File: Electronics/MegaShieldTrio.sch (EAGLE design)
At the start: 29 parts, among them J2 RJ11-2L-B, X1 RJ45-6L21-B, X2 Cruise

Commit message: New sonar board; trio modified to match
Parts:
- removed ADCL2: Analog In 0-7, pinhead:PINHD-1X8
- added COMMUN: Digital 14-21, pinhead:PINHD-1X8
- added JP15: (no value), pinhead:PINHD-1X10
- ADCL: value Digital 14-21 -> Analog In 0-7
- renumbered ADCL1 to PWML
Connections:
- new net N$2: COMMUN.2, PWML.3
- new net N$9: COMMUN.1, PWML.4
- net +5V: now also X1.1; no longer X1.2
- net A6: now also COMMUN.7; no longer ADCL.7
- net D3INT1: now also COMMUN.8; no longer ADCL.8
- net GND: now also X1.4; no longer X1.1
- net N$11: now also COMMUN.4; no longer ADCL.4
- net N$25: now also ADCL.5, X1.7; no longer ADCL2.5, X1.5
- net N$26: now also ADCL.6, X1.3; no longer ADCL2.6, X1.6
- net N$33: now also COMMUN.3; no longer ADCL.3
- net N$34: now also ADCL.7, X1.5; no longer ADCL2.7, X1.7
- net N$35: now also ADCL.8; no longer ADCL2.8
- net N$36: now also X1.2; no longer X1.3
- net N$7: now also ADCL.4, X1.6; no longer ADCL2.4, X1.4
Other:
- note added: "3.3v"
- note added: "3V"
- note added: "D1 (Tx2)"
- note added: "D2 (Rx2)"
- note added: "D3 (MOSI)"
- note added: "D4 (MISO)"
- note added: "D5 (SCK)"
- note added: "D6 (SS)"
- note added: "GND"
- note added: "MISO"
- note added: "MOSI"
- note added: "NCS"
- note added: "NPO"
- note added: "Pgm"
- note added: "RST"
- note added: "Rx"
- note added: "SCLK"
- note added: "Tx"
- moved on the sheet: ADCL, JP11, JP12, JP13

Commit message: Parts match physical size
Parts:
- removed ADCH: Analog In 8-15, pinhead:PINHD-1X8
- removed ADCL: Analog In 0-7, pinhead:PINHD-1X8
- removed ADCL4, PWMH: Digital 8-13, pinhead:PINHD-1X8
- removed COMMUN: Digital 14-21, pinhead:PINHD-1X8
- removed J1: (no value), con-jack:JACK-PLUG0
- removed J2: RJ11-2L-B, con-tycoelectronics:RJ11-2L-B
- removed JP1, JP2: 5V, pinhead:PINHD-1X1
- removed JP10: (no value), pinhead:PINHD-1X4
- removed JP11: (no value), pinhead:PINHD-1X9
- removed JP12, JP13: (no value), pinhead:PINHD-1X2
- removed JP14: (no value), pinhead:PINHD-2X4
- removed JP15: (no value), pinhead:PINHD-1X10
- removed JP3, JP4: GND, pinhead:PINHD-1X1
- removed JP6: C3 Analog, pinhead:PINHD-1X15
- removed JP8: C4 Analog, pinhead:PINHD-1X15
- removed JP9: (no value), pinhead:PINHD-1X6
- removed PWML: Digital 0-7, pinhead:PINHD-1X8
- removed XIOH: Digital 22-37, pinhead:PINHD-2X8
- removed XIOL: Digital 38-53, pinhead:PINHD-2X8
- added C3A: C3 Analog, pinhead:PINHD-1X15
- added C3A2, C3D2, C4A2, C4D2: 1X15HEADER, Elcano:1X15HEADER
- added C4A: C4 Analog, pinhead:PINHD-1X15
- added C4SA0-5: Nano shield, Elcano:1X6HEADER
- added C4SD8-13: Nano shield, Elcano:PINHD-1X8SMALL8
- added C4SPWR: Nano shield, pinhead:PINHD-1X5
- added C5A: C5 Analog, pinhead:PINHD-1X15
- added C6A0-7: C6 Analog In 0-7, pinhead:PINHD-1X8
- added C6A8-15: C6 Analog In 8-15, pinhead:PINHD-1X8
- added C6D0-7: GPS, pinhead:PINHD-1X8
- added C6D14-21: C6 Digital 14-21, pinhead:PINHD-1X8
- added C6D14-21_2: C5D, Elcano:PINHD-1X8SMALL8
- added C6D22-37: C6 Digital 22-37, pinhead:PINHD-2X9
- added C6D38-53: C6 Digital 38-53, pinhead:PINHD-2X9
- added C6D70-77, C6D78-85: Max32, pinhead:PINHD-2X8
- added C6D8-13: C6D8-13, pinhead:PINHD-1X8
- added ICSP: (no value), pinhead:PINHD-2X3
- added MOUSE: Visual odometry, pinhead:PINHD-1X10
- added R2, R3: 1 M, rcl:R-US_0207/10
- added RL1: V23040--B201TSC, Elcano:V23040--B201TSC
- added U$4: CHR_UM6, Elcano:CHR_UM6
- added X3: ODO_JACK, Elcano:ODO_JACK
- added X4, X5: RJ45-8L-B, con-tycoelectronics:RJ45-8L-B
- C4SD0-7: value Digital 0-7 -> Nano shield
- POWER: value POWER -> C6 Power; device pinhead:PINHD-1X6 -> pinhead:PINHD-1X8
- R1: value 1M -> 1 M; device rcl:R-US_0204/5 -> rcl:R-US_0207/10
- X1: value RJ45-6L21-B -> Vehicle control; device con-tycoelectronics:RJ45-6L21-B -> con-subd:M25H
- X2: value Cruise -> ODO_JACK; device con-subd:F25H -> Elcano:ODO_JACK
- renumbered ADCL3 to C4SD0-7, JP5 to C3D, JP7 to C4D
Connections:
- removed net A12: JP6.5, PWMH.1, X2.10
- removed net A13: ADCH.6, C3D.14, X2.6
- removed net A14: ADCH.7, C3D.13, X2.7
- removed net A15: ADCH.8, C3D.12, X2.8
- removed net A6: COMMUN.7, X2.23
- removed net D23: X2.5, XIOH.15
- removed net D27: JP6.15, X2.4, XIOH.11
- removed net D29: ADCL4.6, JP8.15, X2.3, XIOH.9
- removed net D31: X2.2, XIOH.7
- removed net D33: X2.1, XIOH.5
- removed net D35: JP14.7, X2.15, XIOH.3
- removed net D36: X2.13, XIOH.2
- removed net D37: X2.16, XIOH.1
- removed net D3INT1: COMMUN.8, J1.3, R1.2, X2.21
- removed net D43: XIOL.11
- removed net D49: J2.1, XIOL.5
- removed net D53: J2.3, XIOL.1
- removed net D9: JP6.6, PWMH.2
- removed net N$1: PWML.1, X2.19
- removed net N$2: COMMUN.2, PWML.3
- removed net N$27: ADCL4.8, JP8.13
- removed net N$6: J2.4, XIOL.2
- new net AREF: C3A.13, C3A2.13, C4A.13, C4A2.13, C4SD8-13.1, C5A.13, C6D8-13.1
- new net CRS_BRAKE: C3D.13, C3D2.13, C5A.6, C6A8-15.7, X1.7
- new net CRS_DRIVE_CMD: C3D.2, C3D2.2, X1.18
- new net CRS_REVERSE: C3D.11, C3D2.11, C6D22-37.2, X1.13
- new net CRS_STEER: C3D.14, C3D2.14, C5A.7, C6A8-15.6, X1.6
- new net CRS_THROTTLE: C3D.12, C3D2.12, C5A.5, C6A8-15.8, X1.8
- new net DIRECTION: C3A.6, C3A2.6
- new net HORIZ: C4A.5, C4A2.5, C4SA0-5.1
- new net LED1: C6D22-37.15, X1.5
- new net LED3: C3A.15, C3A2.15, C6D22-37.11, X1.4
- new net LED4: C4A.15, C4A2.15, C4SD8-13.3, C6D22-37.9, X1.3
- new net LED5: C6D22-37.7, X1.2
- new net LED6: C6D22-37.5, X1.1
- new net LED7: C6D22-37.3, X1.15
- new net LED8: C6D22-37.1, X1.16
- new net MISO: C6D38-53.13, ICSP.1, MOUSE.5, U$4.7
- new net MOSI: C6D38-53.14, ICSP.4, MOUSE.6, U$4.8
- new net MOUSE_LED: C6D38-53.12, MOUSE.10
- new net MOUSE_SS: C6D38-53.16, MOUSE.4
- new net N$29: C3D.9, C3D2.9, RL1K.2
- new net N$30: C6D78-85.7, C6D78-85.8
- new net N$31: C6D78-85.10, C6D78-85.9
- new net N$32: RL1K1.5, X4.1, X5.1
- new net N$39: C6D78-85.15, C6D78-85.16
- new net N$41: C6D70-77.1, C6D70-77.2
- new net N$42: C6D0-7.6, C6D14-21.2, C6D14-21_2.7, U$4.9
- new net N$43: C6D14-21.6, C6D14-21_2.3, U$4.13
- new net N$44: C6D70-77.3, C6D70-77.4
- new net N$45: C6D70-77.5, C6D70-77.6
- new net N$46: C6D70-77.7, C6D70-77.8
- new net N$47: C6D70-77.10, C6D70-77.9
- new net N$48: C6D70-77.11, C6D70-77.12
- new net N$49: C6D70-77.13, C6D70-77.14
- new net N$50: C6D70-77.15, C6D70-77.16
- new net N$52: C4A.14, C4A2.14
- new net N$54: C3D.6, C3D2.6
- new net N$55: C3D.10, C3D2.10
- new net N$56: C3A.1, C3A2.1, C5A.1, C6D22-37.13, POWER.1
- new net N$57: C3A.7, C3A2.7
- new net N$59: C3A.14, C3A2.14
- new net NPD: C6D38-53.10, MOUSE.9
- new net PRESENCE: C4A.8, C4A2.8, C4SA0-5.4
- new net RX0: C6D0-7.8, X1.22
- new net SCK: C6D38-53.15, ICSP.3, MOUSE.7, U$4.6
- new net SIZE: C4A.7, C4A2.7, C4SA0-5.3
- new net SPEED: C3A.5, C3A2.5, C6D8-13.7, X1.10
- new net SPEED_LIMIT: C4D.7, C4D2.7, C4SD0-7.5, X1.9
- new net TILT_SS: C6D38-53.8, U$4.5
- new net TX0: C6D0-7.7, X1.20
- new net VBIT0: C4D.8, C4D2.8, C4SD0-7.6, C6D38-53.3
- new net VBIT1: C4D.9, C4D2.9, C4SD0-7.7, C6D38-53.5
- new net VBIT2: C4D.10, C4D2.10, C4SD0-7.8, C6D38-53.7
- new net VBIT3: C4D.11, C4D2.11, C4SD8-13.8, C6D38-53.9
- new net VERT: C4A.6, C4A2.6, C4SA0-5.2
- new net VIS_VALID: C4D.15, C4D2.15, C4SD8-13.4, C6D38-53.11
- new net WHEEL_CLICK: C6D14-21.8, C6D14-21_2.1, R2.1, X1.21, X3.1
- new net WIRELESS: C6D14-21.7, C6D14-21_2.2, R1.1, X1.14, X2.1
- net +5V: now also C3A.4, C3A2.4, C4A.4, C4A2.4, C4SPWR.3, C5A.4, C6D22-37.17, C6D22-37.18, ICSP.2, MOUSE.2, POWER.4, R1.2, R2.2, R3.2, RL1K1.6, U$4.1, X1.24; no longer JP1.1, JP10.3, JP2.1, JP6.4, JP8.4, POWER.3, R1.1, X1.1, X2.24
- net D39: now also C6D38-53.2, X1.12; no longer X2.12, XIOL.15
- net D41: now also C6D38-53.4, X1.11; no longer X2.11, XIOL.13
- net GND: now also C3A.2, C3A2.2, C3D2.4, C4A.2, C4A2.2, C4D2.4, C4SD8-13.2, C4SPWR.4, C4SPWR.5, C5A.2, C6D38-53.17, C6D38-53.18, C6D8-13.2, ICSP.6, MOUSE.1, POWER.2, POWER.3, U$4.2, U$4.3, X1.25, X2.2, X2.3, X3.2, X3.3, X4.4, X5.4; no longer ADCL4.7, J1.1, J1.2, J2.6, JP10.4, JP3.1, JP4.1, JP6.2, JP8.2, POWER.4, POWER.5, PWMH.7, X1.4, X2.25
- net N$10: now also C3D2.1, C4D2.2
- net N$11: now also C4D2.5, C6D14-21.4, C6D14-21_2.5; no longer COMMUN.4
- net N$12: now also C3D2.5, C4D2.6
- net N$13: now also C3D.7, C3D2.7, X5.2; no longer C4D.7, C4SD0-7.5
- net N$14: now also C5A.11, C6A8-15.2, X5.7; no longer J2.2, XIOL.3
- net N$15: now also C5A.10, C6A8-15.3, X5.6; no longer C3D.2, X2.18
- net N$16: now also C5A.9, C6A8-15.4, X5.5; no longer JP14.2, JP8.5, JP9.1
- net N$17: now also C6D14-21.5, C6D14-21_2.4, U$4.12; no longer C4D.10, C4SD0-7.8
- net N$18: now also C5A.8, C6A8-15.5, X5.3; no longer ADCL4.1, C4D.11
- net N$19: now also C4D2.12, C4SD8-13.7, C6A0-7.3; no longer ADCL4.2, JP14.1
- net N$20: now also C4D2.14, C4SD8-13.5, C6A0-7.1; no longer ADCL4.4, JP14.5
- net N$21: now also C5A.12, C6A8-15.1, X5.8; no longer JP14.4, JP8.6, JP9.2
- net N$22: now also C4A.1, C4A2.1; no longer JP14.6, JP8.7, JP9.3
- net N$23: now also C6D78-85.1, C6D78-85.2; no longer ADCL4.5, C4D.15
- net N$24: now also C6D78-85.3, C6D78-85.4; no longer JP14.8, JP8.8, JP9.4
- net N$25: now also C3A.9, C3A2.9, C4A.9, C4A2.9, C4SA0-5.5, C6A0-7.5, X4.7; no longer ADCL.5, JP6.9, JP8.9, JP9.5, X1.7
- net N$26: now also C3A.10, C3A2.10, C4A.10, C4A2.10, C4SA0-5.6, C6A0-7.6, X4.3; no longer ADCL.6, JP6.10, JP8.10, JP9.6, X1.3
- net N$28: now also C6D78-85.5, C6D78-85.6; no longer JP10.2, JP8.14
- net N$3: now also C4D2.13, C4SD8-13.6, C6A0-7.2; no longer ADCL4.3, JP14.3
- net N$33: now also C4D2.1, C6D14-21.3, C6D14-21_2.6; no longer COMMUN.3
- net N$34: now also C3A.11, C3A2.11, C4A.11, C4A2.11, C6A0-7.7, X4.5; no longer ADCL.7, JP6.11, JP8.11, X1.5
- net N$35: now also C3A.12, C3A2.12, C4A.12, C4A2.12, C6A0-7.8, X4.8; no longer ADCL.8, JP6.12, JP8.12, X1.8
- net N$36: now also C3D2.8, X4.2; no longer X1.2
- net N$37: now also C6D78-85.11, C6D78-85.12; no longer PWML.2, X2.20
- net N$38: now also C6D78-85.13, C6D78-85.14; no longer C4D.9, C4SD0-7.7
- net N$4: now also C3D2.15, C6D22-37.16, X1.17; no longer X2.17, XIOH.16
- net N$5: now also C4SPWR.2, MOUSE.3, POWER.5, RL1K1.4; no longer ADCH.1, C4D.8, C4SD0-7.6, X2.9
- net N$7: now also C3A.8, C3A2.8, C6A0-7.4, X4.6; no longer ADCL.4, JP6.8, X1.6
- net N$8: now also R3.1, RL1K.1; no longer J2.5, XIOL.4
- net N$9: now also C6D0-7.5, C6D14-21.1, C6D14-21_2.8, U$4.10; no longer COMMUN.1, PWML.4
- net RESET: now also C3A.3, C3A2.3, C3D2.3, C4A.3, C4A2.3, C4D2.3, C4SPWR.1, C5A.3, ICSP.5, MOUSE.8, POWER.6; no longer JP10.1, JP6.3, JP8.3, POWER.1
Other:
- note added: "3.3 V"
- note added: "5 V"
- note added: "5V / 3.3V power"
- note added: "Aref"
- note added: "CH Robotics UM6"
- note added: "Chain_2"
- note added: "D19 Rx1"
- note added: "F2"
- note added: "FL2"
- note added: "FR2"
- note added: "GPS Location"
- note added: "L2"
- note added: "NPD"
- note added: "Power 3/5"
- note added: "Presence"
- note added: "R2"
- note added: "SCK"
- note added: "Tilt SS"
- note added: "Vcc"
- note added: "Vision bit 0"
- note added: "Vision bit 1"
- note added: "Vision bit 2"
- note added: "Vision bit 3"
- note added: "Vision valid"
- note added: "Wireless"
- note removed: "(MOSI)"
- note removed: "3.3v"
- note removed: "Coneness"
- note removed: "D19 Tx1"
- note removed: "Female"
- note removed: "Power F"
- note removed: "SS"
- note removed: "Vision"
- moved on the sheet: R1

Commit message: Rearranged signals
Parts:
- added JP1, JP2, JP3: (no value), jumper:JP2E
- added JP4: (no value), Elcano:PINHD-1X8SMALL8
- ICSP: value (none) -> C6
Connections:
- net N$17 renamed INU_CNTRL
- net N$32 renamed SNR_PWR
- net N$43 renamed INU_BRN
- removed net CRS_BRAKE: C3D.13, C3D2.13, C5A.6, C6A8-15.7, X1.7
- removed net CRS_DRIVE_CMD: C3D.2, C3D2.2, X1.18
- removed net CRS_REVERSE: C3D.11, C3D2.11, C6D22-37.2, X1.13
- removed net CRS_STEER: C3D.14, C3D2.14, C5A.7, C6A8-15.6, X1.6
- removed net CRS_THROTTLE: C3D.12, C3D2.12, C5A.5, C6A8-15.8, X1.8
- removed net DIRECTION: C3A.6, C3A2.6
- removed net HORIZ: C4A.5, C4A2.5, C4SA0-5.1
- removed net MOUSE_LED: C6D38-53.12, MOUSE.10
- removed net N$10: C3D.1, C3D2.1, C4D.2, C4D2.2, C4SD0-7.2
- removed net N$11: C4D.5, C4D2.5, C4SD0-7.3, C6D14-21.4, C6D14-21_2.5
- removed net N$12: C3D.5, C3D2.5, C4D.6, C4D2.6, C4SD0-7.4
- removed net N$13: C3D.7, C3D2.7, X5.2
- removed net N$14: C5A.11, C6A8-15.2, X5.7
- removed net N$15: C5A.10, C6A8-15.3, X5.6
- removed net N$16: C5A.9, C6A8-15.4, X5.5
- removed net N$18: C5A.8, C6A8-15.5, X5.3
- removed net N$19: C4D.12, C4D2.12, C4SD8-13.7, C6A0-7.3
- removed net N$20: C4D.14, C4D2.14, C4SD8-13.5, C6A0-7.1
- removed net N$21: C5A.12, C6A8-15.1, X5.8
- removed net N$22: C4A.1, C4A2.1
- removed net N$25: C3A.9, C3A2.9, C4A.9, C4A2.9, C4SA0-5.5, C6A0-7.5, X4.7
- removed net N$26: C3A.10, C3A2.10, C4A.10, C4A2.10, C4SA0-5.6, C6A0-7.6, X4.3
- removed net N$29: C3D.9, C3D2.9, RL1K.2
- removed net N$3: C4D.13, C4D2.13, C4SD8-13.6, C6A0-7.2
- removed net N$33: C4D.1, C4D2.1, C4SD0-7.1, C6D14-21.3, C6D14-21_2.6
- removed net N$34: C3A.11, C3A2.11, C4A.11, C4A2.11, C6A0-7.7, X4.5
- removed net N$35: C3A.12, C3A2.12, C4A.12, C4A2.12, C6A0-7.8, X4.8
- removed net N$36: C3D.8, C3D2.8, X4.2
- removed net N$42: C6D0-7.6, C6D14-21.2, C6D14-21_2.7, U$4.9
- removed net N$52: C4A.14, C4A2.14
- removed net N$54: C3D.6, C3D2.6
- removed net N$55: C3D.10, C3D2.10
- removed net N$56: C3A.1, C3A2.1, C5A.1, C6D22-37.13, POWER.1
- removed net N$57: C3A.7, C3A2.7
- removed net N$59: C3A.14, C3A2.14
- removed net N$9: C6D0-7.5, C6D14-21.1, C6D14-21_2.8, U$4.10
- removed net PRESENCE: C4A.8, C4A2.8, C4SA0-5.4
- removed net RX0: C6D0-7.8, X1.22
- removed net SIZE: C4A.7, C4A2.7, C4SA0-5.3
- removed net SPEED_LIMIT: C4D.7, C4D2.7, C4SD0-7.5, X1.9
- removed net TILT_SS: C6D38-53.8, U$4.5
- removed net TX0: C6D0-7.7, X1.20
- removed net VBIT2: C4D.10, C4D2.10, C4SD0-7.8, C6D38-53.7
- removed net VBIT3: C4D.11, C4D2.11, C4SD8-13.8, C6D38-53.9
- removed net VERT: C4A.6, C4A2.6, C4SA0-5.2
- removed net VIS_VALID: C4D.15, C4D2.15, C4SD8-13.4, C6D38-53.11
- removed net WHEEL_CLICK: C6D14-21.8, C6D14-21_2.1, R2.1, X1.21, X3.1
- removed net WIRELESS: C6D14-21.7, C6D14-21_2.2, R1.1, X1.14, X2.1
- new net 3.3V: C3A.14, C3A2.14, C4A.14, C4A2.14, C4SPWR.2, MOUSE.3, POWER.5, RL1K1.4
- new net 4D5_6A14: C4D.8, C4D2.8, C4SD0-7.6
- new net 4D6_6A15: C4D.9, C4D2.9, C4SD0-7.7
- new net 4D7_6D43: C4D.10, C4D2.10, C4SD0-7.8, C6D38-53.6
- new net 6D10_2A6: C6D8-13.6, X1.23
- new net C2STAT: C6D14-21.4, C6D14-21_2.5, X1.19
- new net C4AVL: C3D.5, C3D2.5, C4D.6, C4D2.6, C4SD0-7.4, C6D22-37.3
- new net C4D11: C4D.14, C4D2.14, C4SD8-13.5
- new net C4D12: C4D.15, C4D2.15, C4SD8-13.4
- new net C6AVL: C4D.5, C4D2.5, C4SD0-7.3, C6D22-37.16
- new net C6D29: C6D22-37.10, JP4.1
- new net C6D31: C6D22-37.8, JP4.2
- new net C6D33: C6D22-37.6, JP4.3
- new net C6D35: C6D22-37.4, JP4.4
- new net C6D37: C6D22-37.2, JP4.5
- new net CHN1: C3D.7, C3D2.7, C6D38-53.1, X4.2
- new net CHN2: C3D.6, C3D2.6, C6D22-37.1, X5.2
- new net CLICK1: C6D0-7.6, R2.1, X1.21, X3.1
- new net CLICK2: C6D0-7.5, R1.1, X1.14, X2.1
- new net CRS_BRK: C3D.8, C3D2.8, C6A0-7.6, C6D0-7.3, C6D38-53.3, X1.7
- new net CRS_REV: C3D.11, C3D2.11, C6D38-53.9, X1.13
- new net CRS_STR: C3D.9, C3D2.9, C6A0-7.7, C6D38-53.5, X1.6
- new net CRS_THR: C3D.12, C3D2.12, C6A0-7.8, C6D38-53.11, C6D38-53.8, X1.8
- new net DRV_CMD: C3D.1, C3D2.1, C6D22-37.11, X1.18
- new net F2RNG: C3A.10, C3A2.10, C4A.10, C4A2.10, C4SA0-5.6, C5A.5, C6A8-15.8, X5.4
- new net FL2RNG: C5A.6, C6A8-15.7, X5.5
- new net FL_RNG: C3A.6, C3A2.6, C4A.6, C4A2.6, C4SA0-5.2, C6A0-7.2, X4.5
- new net FR2RNG: C5A.7, C6A8-15.6, X5.6
- new net FR_RNG: C3A.7, C3A2.7, C4A.7, C4A2.7, C4SA0-5.3, C6A0-7.3, X4.6
- new net F_RNG: C3A.5, C3A2.5, C4A.5, C4A2.5, C4SA0-5.1, C5A.10, C6A0-7.1, X4.4
- new net GPS_CNTRL: C6D14-21.1, C6D14-21_2.8, U$4.10
- new net GPS_LOC: C6D14-21.2, C6D14-21_2.7, U$4.9
- new net GPS_PWR: C6D8-13.7
- new net INU_SS: C6D22-37.12, U$4.5
- new net L2RNG: C3A.11, C3A2.11, C4A.11, C4A2.11, C5A.8, X5.7
- new net L_RNG: C3A.8, C3A2.8, C4A.8, C4A2.8, C4SA0-5.4, C5A.11, C6A0-7.4, X4.7
- new net MOV_OK: C3D.13, C3D2.13, C4SD0-7.5, C6D0-7.4, JP3.3, X1.17
- new net N$1: C4A.3, C4A2.3, C4D.3, C4D2.3, C4SPWR.1
- new net N$2: C4D.7, C4D2.7
- new net N$6: C6D38-53.17, JP2.2
- new net NAV_FIX: C4D.2, C4D2.2, C4SD0-7.1, C6D14-21.3, C6D14-21_2.6
- new net PATH: C3D.2, C3D2.2, C4D.1, C4D2.1, C4SD0-7.2, C6D22-37.9
- new net PWR_SEL: C3D.10, C3D2.10, C6D38-53.7, RL1K.2
- new net R2RNG: C3A.12, C3A2.12, C4A.12, C4A2.12, C5A.9, C6A8-15.4, X5.8
- new net R_RNG: C3A.9, C3A2.9, C4A.9, C4A2.9, C4SA0-5.5, C5A.12, C6A0-7.5, X4.8
- new net SPD_LMT: C4D.12, C4D2.12, C4SD8-13.7, X1.9
- new net VIN: C3A.1, C3A2.1, C4A.1, C4A2.1, C5A.1, C6D22-37.14, POWER.1
- new net VIS_IN: X1.20
- new net VIS_OUT: C6D0-7.7, X1.22
- net +5V: no longer C5A.4, R3.2
- net D39: now also C3D.15, C3D2.15, C4D.13, C4D2.13, C4SD8-13.6, JP4.6
- net D41: now also C4D.11, C4D2.11, C4SD8-13.8, JP2.3, JP4.7
- net GND: now also C6D22-37.5, JP2.1, X4.3, X5.3; no longer C6D38-53.17, X4.4, X5.4
- net LED1: now also C6D8-13.8; no longer C6D22-37.15
- net LED3: no longer C6D22-37.11
- net LED4: no longer C6D22-37.9
- net LED5: now also C5A.15, C6D38-53.12, MOUSE.10; no longer C6D22-37.7
- net LED6: now also C6D22-37.13; no longer C6D22-37.5
- net LED7: now also C6D22-37.15; no longer C6D22-37.3
- net LED8: now also C6D14-21.8, C6D14-21_2.1; no longer C6D22-37.1
- net MISO: now also C6D8-13.4, JP3.1; no longer C6D38-53.13
- net MOSI: now also C6D8-13.5
- net N$4: now also C6D38-53.15, JP1.2; no longer C3D.15, C3D2.15, C6D22-37.16, X1.17
- net N$5: now also C6D38-53.13, JP3.2; no longer C4SPWR.2, MOUSE.3, POWER.5, RL1K1.4
- net N$7: now also C6D14-21.7, C6D14-21_2.2; no longer C3A.8, C3A2.8, C6A0-7.4, X4.6
- net RESET: now also C6D22-37.7; no longer C4A.3, C4A2.3, C4D.3, C4D2.3, C4SPWR.1
- net SCK: now also C6D8-13.3, JP1.1; no longer C6D38-53.15
- net SPEED: now also C3D.14, C3D2.14, C6A8-15.3, JP1.3; no longer C3A.5, C3A2.5, C6D8-13.7
- net VBIT0: now also C6A8-15.2; no longer C4D.8, C4D2.8, C4SD0-7.6, C6D38-53.3
- net VBIT1: now also C6A8-15.1; no longer C4D.9, C4D2.9, C4SD0-7.7, C6D38-53.5
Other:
- note added: "A12"
- note added: "C2 Status"
- note added: "C4 MISO"
- note added: "C4 MOSI"
- note added: "C6 Avail"
- note added: "Chaining 1"
- note added: "Click 2"
- note added: "Cruise reverse"
- note added: "D39"
- note added: "D39 Spare"
- note added: "D41"
- note added: "D41 Spare"
- note added: "D44"
- note added: "Drive Command"
- note added: "F2 RNG"
- note added: "INU SS"
- note added: "L2 RNG"
- note added: "Power Select"
- note added: "R2 RNG"
- note added: "Rx D0"
- note added: "SPARE D39"
- note added: "Spare"
- note added: "Tx D1"
- note added: "V In"
- note added: "VCC"
- note added: "Vision In"
- note added: "Vision Out"
- note added: "Vision in"
- note removed: "C6"
- note removed: "C6 Data"
- note removed: "Directn"
- note removed: "Exp Horiz"
- note removed: "Exp Size"
- note removed: "Exp Vert"
- note removed: "Gamebots Cmd"
- note removed: "Horiz"
- note removed: "LED 1"
- note removed: "Presence"
- note removed: "Reserved"
- note removed: "Reverse Cmd Out"
- note removed: "Rx D1"
- note removed: "Rx0"
- note removed: "Size"
- note removed: "Tx D0"
- note removed: "Vert"
- note removed: "Vision bit 0"
- note removed: "Vision bit 1"
- note removed: "Vision bit 2"
- note removed: "Vision bit 3"
- note removed: "Vision valid"
- moved on the sheet: C4SA0-5, C6A8-15, C6D0-7, C6D38-53, C6D70-77, C6D78-85, C6D8-13, ICSP, MOUSE, POWER, U$4, X4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

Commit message: Power and ground traces
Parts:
- JP1: value (none) -> D52/12
- JP2: value (none) -> D50/11
- JP3: value (none) -> D48/10
- JP4: value (none) -> Spares
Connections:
- removed net GPS_PWR: C6D8-13.7
- removed net N$1: C4A.3, C4A2.3, C4D.3, C4D2.3, C4SPWR.1
- removed net N$2: C4D.7, C4D2.7
- removed net VBIT0: C6A8-15.2
- removed net VBIT1: C6A8-15.1
- new net N$3: C6D38-53.6, JP4.8
- net +5V: now also R3.2
- net 4D5_6A14: now also C6A8-15.2
- net 4D6_6A15: now also C6A8-15.1
- net 4D7_6D43: no longer C6D38-53.6
- net CRS_STR: now also C6D0-7.2
- net D41: now also JP1.3; no longer JP2.3
- net GND: now also JP1.1; no longer JP2.1
- net L2RNG: now also C6A8-15.5
- net MOV_OK: now also C4D.7, C4D2.7
- net N$4: now also JP2.2; no longer JP1.2
- net N$6: now also JP1.2; no longer JP2.2
- net RESET: now also C4A.3, C4A2.3, C4D.3, C4D2.3, C4SPWR.1
- net SCK: now also JP2.1; no longer JP1.1
- net SPEED: now also JP2.3; no longer JP1.3
- net VIS_IN: now also C6D0-7.8
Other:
- note added: "F_RNG"
- note added: "L_RNG"
- note added: "R_RNG"
- note removed: "AREF"
- note removed: "Aref"
- note removed: "C6 Avail"
- note removed: "D41"
- note removed: "F range"
- note removed: "F2"
- note removed: "F2 RNG"
- note removed: "FL2"
- note removed: "FR2"
- note removed: "L2"
- note removed: "L2 RNG"
- note removed: "Move OK"
- note removed: "R2"
- note removed: "R2 RNG"
- note removed: "Tx0"
- note removed: "V In"
- note removed: "VCC"
- moved on the sheet: C3A2, C4A2, C4SA0-5, JP1, JP2

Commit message: Routed
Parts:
- C6D14-21: device pinhead:PINHD-1X8 -> Elcano:PINHD-1X8SMALL8
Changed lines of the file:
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@@
 <setting verticaltext="up"/>
 </settings>
-<grid distance="0.05" unitdist="inch" unit="inch" style="lines" multiple="1" display="no" altdistance="0.01" altunitdist="inch" altunit="inch"/>
+<grid distance="0.1" unitdist="inch" unit="inch" style="lines" multiple="1" display="no" altdistance="0.01" altunitdist="inch" altunit="inch"/>
 <layers>
 <layer number="1" name="Top" color="4" fill="1" visible="no" active="no"/>
@@
 <parts>
 <part name="GND5" library="supply1" deviceset="GND" device=""/>
-<part name="C6D14-21" library="pinhead" deviceset="PINHD-1X8" device="" value="C6 Digital 14-21"/>
+<part name="C6D14-21" library="Elcano" deviceset="PINHD-1X8" device="SMALL8" value="C6 Digital 14-21"/>
 <part name="C6A8-15" library="pinhead" deviceset="PINHD-1X8" device="" value="C6 Analog In 8-15"/>
 <part name="C6D22-37" library="pinhead" deviceset="PINHD-2X9" device="" value="C6 Digital 22-37"/>

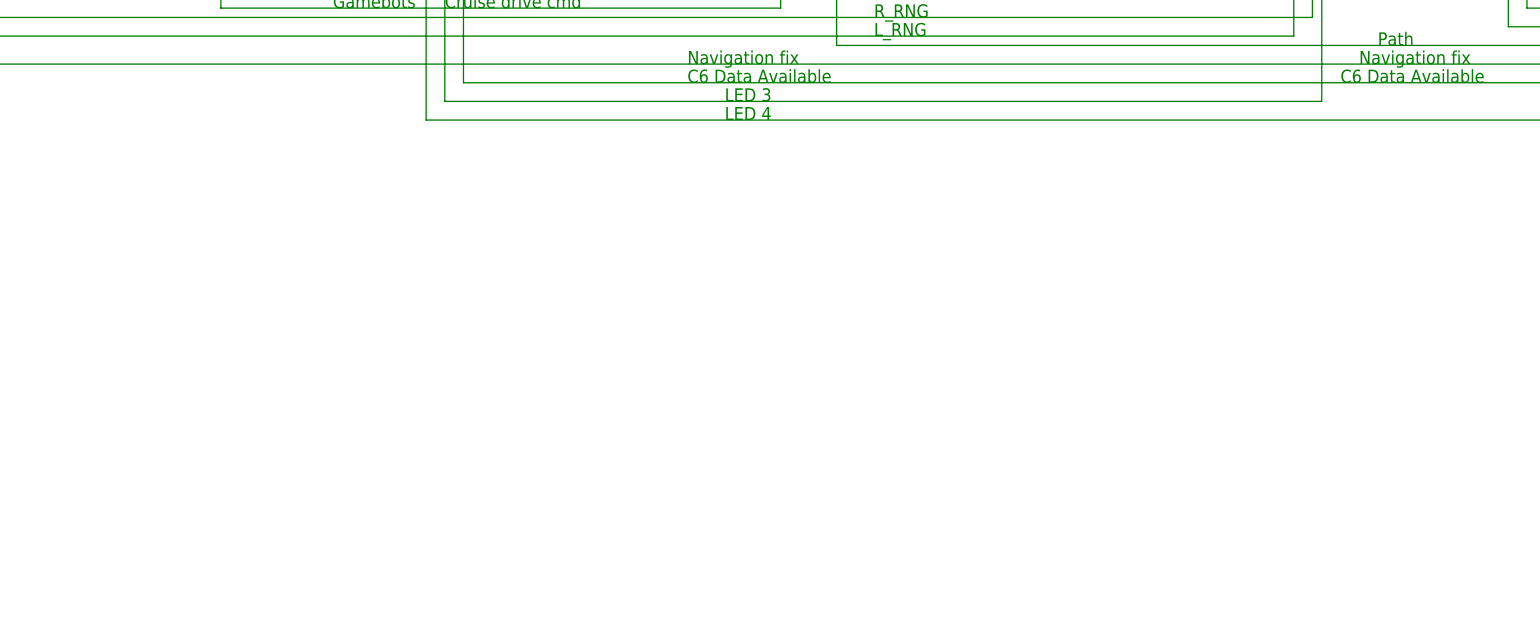
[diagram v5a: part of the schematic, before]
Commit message: Proto area; thickened traces
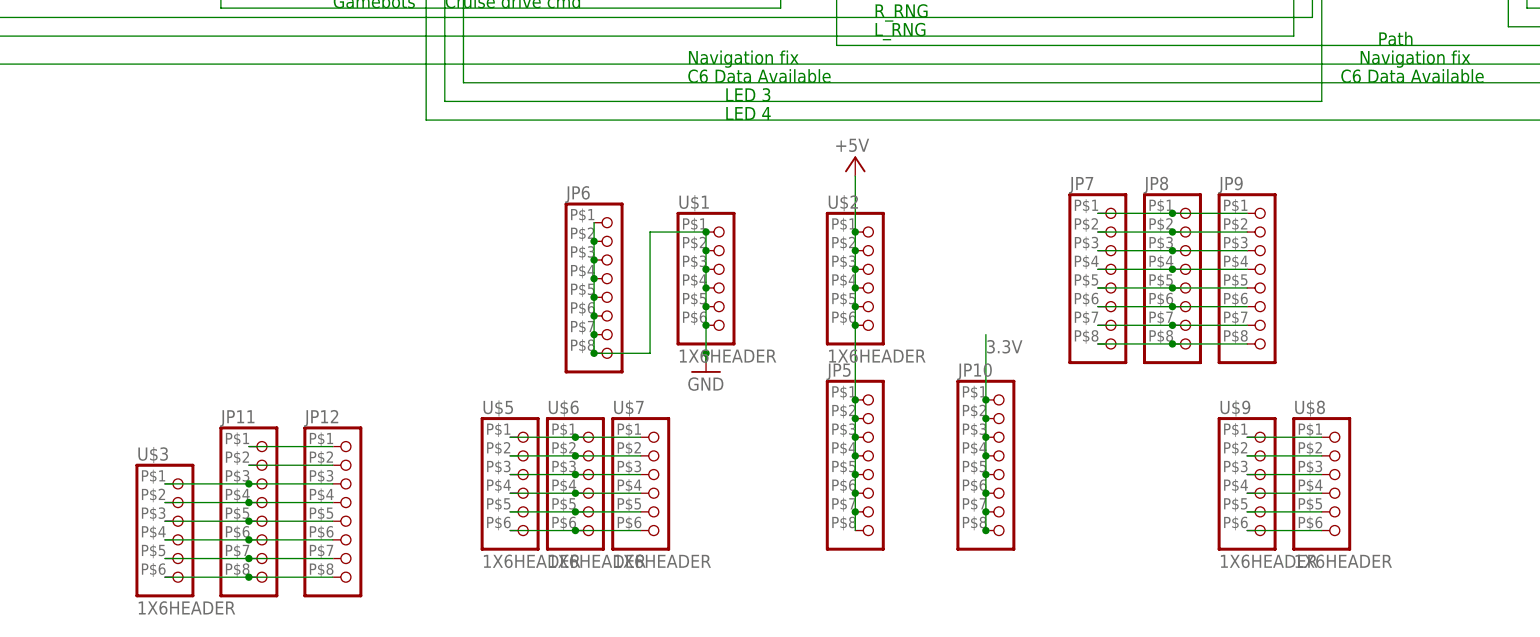
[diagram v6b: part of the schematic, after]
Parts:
- added JP10, JP11, JP12, JP5, JP6, JP7, JP8, JP9: (no value), Elcano:PINHD-1X8SMALL8
- added U$1, U$2, U$3, U$5, U$6, U$7, U$8, U$9: 1X6HEADER, Elcano:1X6HEADER
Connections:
- new net N$1: JP11.1, JP12.1
- new net N$10: JP11.3, JP12.3, U$3.1
- new net N$11: JP11.4, JP12.4, U$3.2
- new net N$12: JP11.5, JP12.5, U$3.3
- new net N$13: JP11.6, JP12.6, U$3.4
- new net N$14: JP11.7, JP12.7, U$3.5
- new net N$15: JP11.8, JP12.8, U$3.6
- new net N$16: U$5.1, U$6.1, U$7.1
- new net N$17: U$5.2, U$6.2, U$7.2
- new net N$18: U$5.3, U$6.3, U$7.3
- new net N$19: U$5.4, U$6.4, U$7.4
- new net N$2: JP11.2, JP12.2
- new net N$20: U$5.5, U$6.5, U$7.5
- new net N$21: U$5.6, U$6.6, U$7.6
- new net N$22: JP7.1, JP8.1, JP9.1
- new net N$25: JP7.2, JP8.2, JP9.2
- new net N$26: JP7.3, JP8.3, JP9.3
- new net N$27: JP7.4, JP8.4, JP9.4
- new net N$29: JP7.5, JP8.5, JP9.5
- new net N$32: JP7.6, JP8.6, JP9.6
- new net N$33: JP7.7, JP8.7, JP9.7
- new net N$34: JP7.8, JP8.8, JP9.8
- new net N$35: U$8.1, U$9.1
- new net N$36: U$8.2, U$9.2
- new net N$40: U$8.3, U$9.3
- new net N$42: U$8.4, U$9.4
- new net N$43: U$8.5, U$9.5
- new net N$51: U$8.6, U$9.6
- net +5V: now also JP5.1, JP5.2, JP5.3, JP5.4, JP5.5, JP5.6, JP5.7, JP5.8, U$2.1, U$2.2, U$2.3, U$2.4, U$2.5, U$2.6
- net 3.3V: now also JP10.1, JP10.2, JP10.3, JP10.4, JP10.5, JP10.6, JP10.7, JP10.8
- net GND: now also JP6.1, JP6.2, JP6.3, JP6.4, JP6.5, JP6.6, JP6.7, JP6.8, U$1.1, U$1.2, U$1.3, U$1.4, U$1.5, U$1.6

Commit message: Rear facing sonars; angles adjusted
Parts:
- 3V: value (none) -> (none)
- 5V_BUS, R1B, R2A, R3A, R5A: value 1X6HEADER -> (none)
- C3A: value C3 Analog -> (none)
- C3A2, C4A2, C4D2: value 1X15HEADER -> (none)
- C4A: value C4 Analog -> (none)
- C4D: value C4 Digital -> (none)
- C4_SHIELD_8-13: value Nano shield -> (none)
- C6A8-15: value C6 Analog In 8-15 -> (none)
- JP1: value D52/12 -> (none)
- JP2: value D50/11 -> (none)
- R4A: value 1X6HEADER -> Proto
- X2: value ODO_JACK -> 2odo__
- X3: value ODO_JACK -> 1odo__
- renumbered C4SD8-13 to C4_SHIELD_8-13, JP10 to 3V, JP11 to R2B, JP12 to R3B, JP5 to 5VBUS, JP6 to GRND, JP7 to R4B, JP8 to R5B, JP9 to R6B, U$1 to GROUND, U$2 to 5V_BUS, U$3 to R1B, U$4 to INU, U$5 to R4A, U$6 to R5A, U$7 to R6A, U$8 to R2A, U$9 to R3A
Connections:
- net N$27 renamed R5B
